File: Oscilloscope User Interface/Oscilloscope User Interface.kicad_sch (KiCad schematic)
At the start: 13 parts, among them J1 Vin, SW1 Shifting, SW2 Scaling, SW3 Trigger

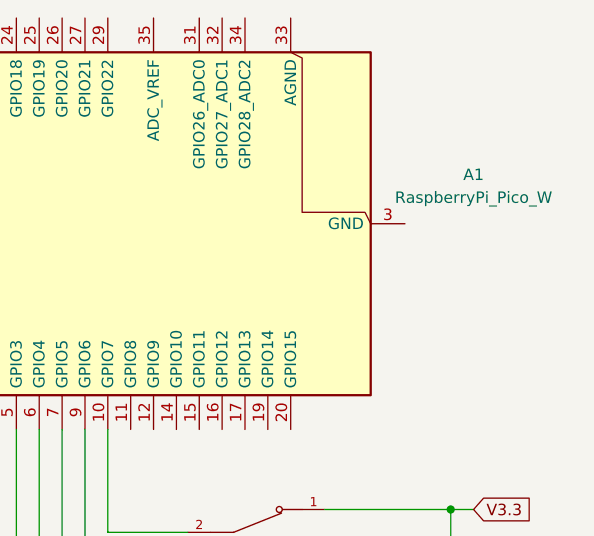
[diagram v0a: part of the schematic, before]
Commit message: "Updated UI schematic"
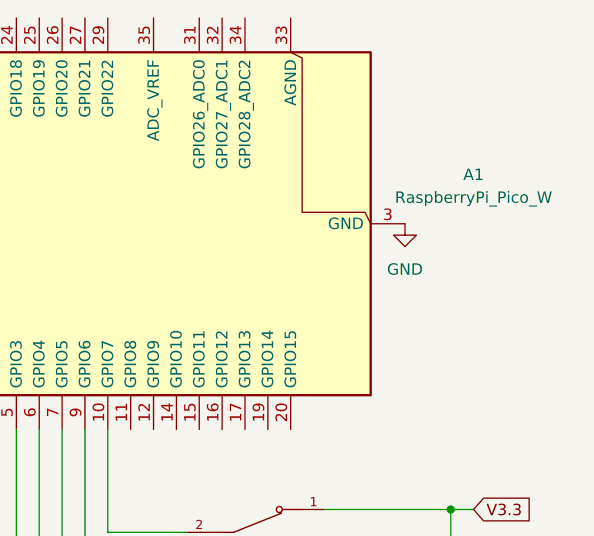
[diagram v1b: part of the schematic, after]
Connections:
- net GND: now also A1.13 (GND), A1.18 (GND), A1.23 (GND), A1.28 (GND), A1.3 (GND), A1.38 (GND), A1.8 (GND)
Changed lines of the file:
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@@
+	)
+	(symbol
+		(lib_id "power:GND")
+		(at 148.59 57.15 0)
+		(unit 1)
+		(body_style 1)
+		(exclude_from_sim no)
+		(in_bom yes)
+		(on_board yes)
+		(in_pos_files yes)
+		(dnp no)
+		(fields_autoplaced yes)
+		(property "Reference" "#PWR04"
+			(at 148.59 63.5 0)
+			(hide yes)
+			(show_name no)
+			(do_not_autoplace no)
+			(effects
+				(font
+					(size 1.27 1.27)
+				)
+			)
+		)
+		(property "Value" "GND"
+			(at 148.59 62.23 0)
+			(show_name no)
+			(do_not_autoplace no)
+			(effects
+				(font
+					(size 1.27 1.27)
+				)
+			)
+		)
+		(property "Footprint" ""
+			(at 148.59 57.15 0)
+			(hide yes)
+			(show_name no)
+			(do_not_autoplace no)
+			(effects
+				(font
+					(size 1.27 1.27)
+				)
+			)
+		)
+		(property "Datasheet" ""
+			(at 148.59 57.15 0)
+			(hide yes)
+			(show_name no)
+			(do_not_autoplace no)
+			(effects
+				(font
+					(size 1.27 1.27)
+				)
+			)
+		)
+		(property "Description" "Power symbol creates a global label with name \"GND\" , ground"
+			(at 148.59 57.15 0)
+			(hide yes)
+			(show_name no)
+			(do_not_autoplace no)
+			(effects
+				(font
+					(size 1.27 1.27)
+				)
+			)
+		)
+		(pin "1"
+		)
+		(instances
+			(project "Oscilloscope User Interface"
+				(path "/3b636a72-d035-4d37-8acb-18971100d3ce"
+					(reference "#PWR04")
+					(unit 1)
+				)
+			)
+		)
 	)
 	(symbol

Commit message: schematic
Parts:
- removed J1: Vin, Connector_PinHeader_2.54mm:PinHeader_1x02_P2.54mm_Vertical, symbol Connector_Generic:Conn_01x02
- added J6, J8, J9: Conn_01x01_Socket, Connector_PinSocket_2.54mm:PinSocket_1x01_P2.54mm_Vertical, symbol Connector:Conn_01x01_Socket
- added J7: Conn_01x08_Socket, Connector_PinSocket_2.54mm:PinSocket_1x08_P2.54mm_Vertical, symbol Connector:Conn_01x08_Socket
- A1: now left out of the parts list
- S1, S2: footprint MINI-SPDT-SW:SW_MINI-SPDT-SW -> SDW:SW_MINI-SPDT-SW
- renumbered R1 to R30, R2 to R31, R3 to R32, R4 to R33, R5 to R34, R6 to R35
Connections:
- net V3.3: now also J8.1 (Pin_1); no longer A1.36 (3V3)
- net at R31.2, SW1.B: now also J7.1 (Pin_1); no longer A1.1 (GPIO0)
- net at R34.2, SW3.A: now also J7.6 (Pin_6); no longer A1.7 (GPIO5)
- net at R32.2, SW2.A: now also J7.4 (Pin_4); no longer A1.5 (GPIO3)
- net at R33.2, SW2.B: now also J7.3 (Pin_3); no longer A1.4 (GPIO2)
- net at S1.2: now also J7.8 (Pin_8); no longer A1.10 (GPIO7)
- net at R30.2, SW1.A: now also J7.2 (Pin_2); no longer A1.2 (GPIO1)
- net at R35.2, SW3.B: now also J7.5 (Pin_5); no longer A1.6 (GPIO4)
- net at S2.2: now also J7.7 (Pin_7); no longer A1.9 (GPIO6)
- net GND: no longer names the net of A1.13 (GND), A1.18 (GND), A1.23 (GND), A1.28 (GND), A1.3 (GND), A1.38 (GND), A1.8 (GND)
- net GND: no longer S1.3, S2.3, SW1.C, SW2.C, SW3.C
- new net 5V: J6.1 (Pin_1)
- new net Ground: J9.1 (Pin_1), S1.3, S2.3, SW1.C, SW2.C, SW3.C
